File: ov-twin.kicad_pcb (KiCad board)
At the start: 4 copper layers, 64 x 64 mm, 101 parts, among them J1 USB_C_Receptacle_USB2.0, J2 Conn_01x02, J3 Conn_01x02, SW1 SW_SPST, SW2 SW_SPST, SW3 SW_SPST, SW4 SW_SPST, SW5 SW_SPST, SW6 SW_SPST, SW7 SW_SPST, SW8 SW_SPST, U1 NCP1117-3.3_SOT223, U2 RP2040, U3 RP2040, U4 W25Q128JVS, U5 W25Q128JVS, U7 LIS3DH, U8 SN74LVC1T45DBV, Y1 Crystal_GND24, Y2 Crystal_GND24, Y3 Crystal_GND24

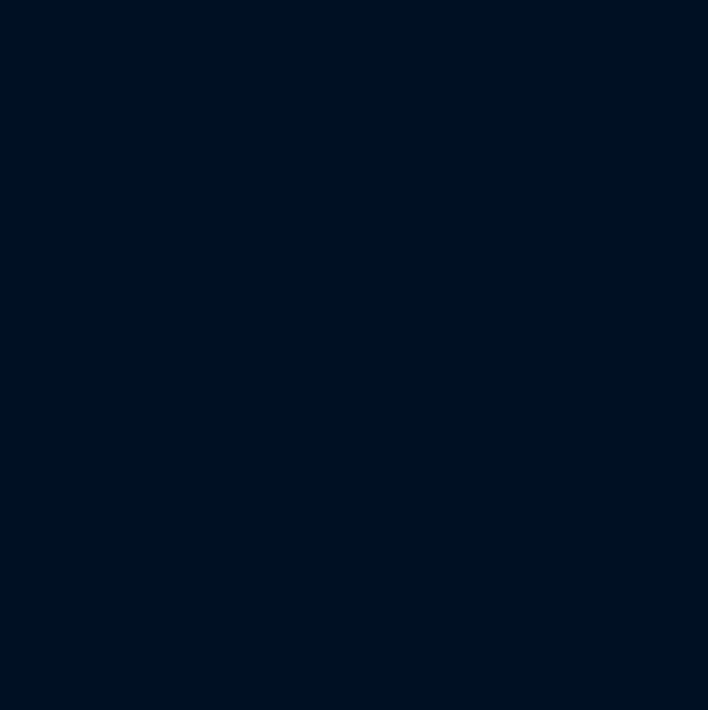
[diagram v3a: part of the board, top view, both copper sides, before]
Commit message: Add missing decoupling and such
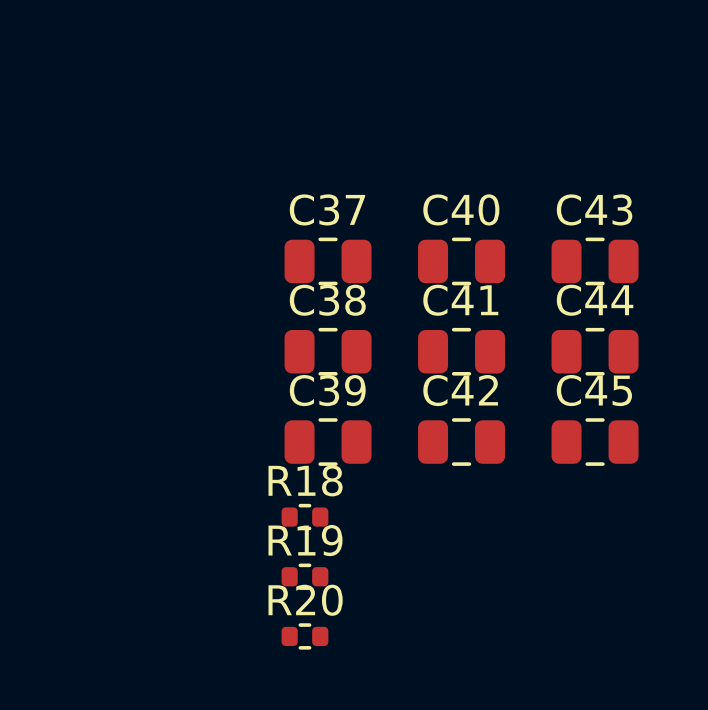
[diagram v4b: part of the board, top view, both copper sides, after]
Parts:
- added C37: 1u, Capacitor_SMD:C_0805_2012Metric, F.Cu at (233.9, 112.2)
- added C38: 1u, Capacitor_SMD:C_0805_2012Metric, F.Cu at (233.9, 115.2)
- added C39: 1u, Capacitor_SMD:C_0805_2012Metric, F.Cu at (233.9, 118.2)
- added C40: 10u, Capacitor_SMD:C_0805_2012Metric, F.Cu at (238.4, 112.2)
- added C41: 10u, Capacitor_SMD:C_0805_2012Metric, F.Cu at (238.4, 115.2)
- added C42: 10u, Capacitor_SMD:C_0805_2012Metric, F.Cu at (238.4, 118.2)
- added C43: 10u, Capacitor_SMD:C_0805_2012Metric, F.Cu at (242.8, 112.2)
- added C44: 10u, Capacitor_SMD:C_0805_2012Metric, F.Cu at (242.8, 115.2)
- added C45: 10u, Capacitor_SMD:C_0805_2012Metric, F.Cu at (242.8, 118.2)
- added R18: 10k, Resistor_SMD:R_0402_1005Metric, F.Cu at (233.2, 120.7)
- added R19: 10k, Resistor_SMD:R_0402_1005Metric, F.Cu at (233.2, 122.7)
- added R20: 10k, Resistor_SMD:R_0402_1005Metric, F.Cu at (233.2, 124.7)
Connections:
- U2 pad 12: unconnected-(U2-GPIO9-Pad12) -> /smartled-3v3
- U2 pad 13: unconnected-(U2-GPIO10-Pad13) -> /lis3dh-sdo-sa0
- U2 pad 14: unconnected-(U2-GPIO11-Pad14) -> /lis3dh-cs
- U2 pad 15: unconnected-(U2-GPIO12-Pad15) -> /lis3dh-scl-spc
- U2 pad 16: unconnected-(U2-GPIO13-Pad16) -> /lis3dh-sdi-sda
- U2 pad 17: unconnected-(U2-GPIO14-Pad17) -> /lis3dh-sdi-sda
- U2 pad 18: unconnected-(U2-GPIO15-Pad18) -> /lis3dh-scl-spc
- U2 pad 27: unconnected-(U2-GPIO16-Pad27) -> /lis3dh-int2
- U2 pad 28: unconnected-(U2-GPIO17-Pad28) -> /lis3dh-int1
- U2 pad 29: unconnected-(U2-GPIO18-Pad29) -> /pi-b-sw-1
- U2 pad 30: unconnected-(U2-GPIO19-Pad30) -> /pi-b-sw-2
- U2 pad 31: unconnected-(U2-GPIO20-Pad31) -> /pi-b-sw-3
- U2 pad 32: unconnected-(U2-GPIO21-Pad32) -> /pi-b-sw-4
- U2 pad 34: unconnected-(U2-GPIO22-Pad34) -> /pi-b-sw-5
- U2 pad 35: unconnected-(U2-GPIO23-Pad35) -> /pi-b-sw-6
- U2 pad 36: unconnected-(U2-GPIO24-Pad36) -> /pi-b-sw-7
- U2 pad 37: unconnected-(U2-GPIO25-Pad37) -> /pi-b-sw-8
- U2 pad 38: unconnected-(U2-GPIO26_ADC0-Pad38) -> /pi-b-pot

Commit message: That worked pretty well I thought!
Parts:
- C37, C38, C39: footprint Capacitor_SMD:C_0805_2012Metric -> Capacitor_SMD:C_0402_1005Metric
- moved C45 113.7 mm to (144.0, 62.0), turned to 180 degrees
- moved C44 102.0 mm to (144.0, 90.0), turned to 180 degrees
- moved C43 85.3 mm to (157.6, 110.0), turned to -90 degrees
- moved C37 65.9 mm to (172.0, 89.6), turned to 180 degrees
- moved R20 64.7 mm to (178.2, 90.6), turned to 90 degrees
- moved C40 63.1 mm to (200.0, 62.1)
- moved R19 62.8 mm to (179.2, 90.6), turned to 90 degrees
- moved C39 62.7 mm to (194.8, 69.2)
- moved R18 60.9 mm to (180.2, 90.6), turned to 90 degrees
- moved C38 56.5 mm to (194.8, 74.4)
- moved C42 53.4 mm to (185.6, 110.0), turned to 90 degrees
- moved C41 45.9 mm to (200.0, 90.0)
- moved C31 5.77 mm to (185.3, 72.5)
- moved R11 5.77 mm to (182.6, 73.0)
- moved R12 5.77 mm to (180.6, 73.0)
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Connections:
- C37 pad 1: +3V3 -> GND
- C37 pad 2: GND -> +3V3
- C38 pad 1: +3V3 -> GND
- C38 pad 2: GND -> +3V3
- C39 pad 1: +5V -> GND
- C39 pad 2: GND -> +5V
- U2 pad 11: unconnected-(U2-GPIO8-Pad11) -> /lis3dh-int1
- U2 pad 17: /lis3dh-sdi-sda -> unconnected-(U2-GPIO14-Pad17)
- U2 pad 18: /lis3dh-scl-spc -> unconnected-(U2-GPIO15-Pad18)
- U2 pad 27: /lis3dh-int2 -> unconnected-(U2-GPIO16-Pad27)
- U2 pad 28: /lis3dh-int1 -> unconnected-(U2-GPIO17-Pad28)
- U2 pad 29: /pi-b-sw-1 -> /pi-b-sw-4
- U2 pad 30: /pi-b-sw-2 -> /pi-b-sw-3
- U2 pad 31: /pi-b-sw-3 -> /pi-b-sw-2
- U2 pad 32: /pi-b-sw-4 -> /pi-b-sw-1
- U2 pad 9: unconnected-(U2-GPIO7-Pad9) -> /lis3dh-int2
- U8 pad 2: Net-(U8-DIR) -> GND
- U8 pad 3: /smartled-5v -> /smartled-5v0
- U8 pad 5: Net-(U8-DIR) -> GND
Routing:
- net +3V3: track 79.3 -> 375.6 mm, vias 33 -> 36
- net /smartled-3v3: track 8.34 -> 73.4 mm, vias 2 -> 5
- net /pi-b-sw-8: track 25.3 -> 71.0 mm, vias 2 -> 5
- net /pi-b-sw-6: track 19.2 -> 60.6 mm, vias 2 -> 6
- net /pi-b-sw-5: track 12.2 -> 53.0 mm, vias 2 -> 4
- net /pi-b-sw-4: track 43.8 -> 83.3 mm, vias 2 -> 5
- net /pi-b-sw-7: track 25.8 -> 64.0 mm, vias 2 -> 5
- net /pi-b-sw-2: track 46.3 -> 81.5 mm, vias 2 -> 5
- net /pi-b-sw-3: track 35.4 -> 65.4 mm, vias 2 -> 5
- net /lis3dh-cs: track 16.7 -> 46.0 mm, vias 2 -> 4
- net /lis3dh-sdo-sa0: track 16.6 -> 45.6 mm, vias 2 -> 4
- net /lis3dh-int2: track 13.0 -> 41.2 mm, vias 2 -> 4
- net /pi-b-pot: track 41.3 -> 69.4 mm, vias 1 -> 3
- net /lis3dh-int1: track 11.9 -> 38.7 mm, vias 2 -> 4
- net GND: track 49.3 -> 73.4 mm, vias 26 -> 30
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- removed copper zone on In2.Cu, net +3V3

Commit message: Updates
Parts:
- removed JP1: SolderJumper_2_Open, Jumper:SolderJumper-2_P1.3mm_Open_TrianglePad1.0x1.5mm
- removed R16, R17: 27, Resistor_SMD:R_0402_1005Metric
- added D25: LED3, LED_SMD:LED_0603_1608Metric, F.Cu at (141.5, 56.0)
- added D26: LED1, LED_SMD:LED_0603_1608Metric, F.Cu at (141.5, 57.5)
- added D27: LEDActive, LED_SMD:LED_0603_1608Metric, F.Cu at (139.5, 59.0)
- added G***: LOGO, LOGO, F.Cu at (141.0, 105.9)
- added J4: Conn_01x02, Connector_PinHeader_2.54mm:PinHeader_1x02_P2.54mm_Vertical, F.Cu at (160.4, 65.4)
- added R21: 220, Resistor_SMD:R_0402_1005Metric, F.Cu at (139.0, 56.0)
- added R22: 220, Resistor_SMD:R_0402_1005Metric, F.Cu at (139.0, 57.5)
- added R23: 470, Resistor_SMD:R_0402_1005Metric, F.Cu at (142.0, 59.0)
- added TP2: TestPoint, TestPoint:TestPoint_Pad_D1.5mm, B.Cu at (167.0, 65.0)
- added TP4: TestPoint, TestPoint:TestPoint_Pad_D1.5mm, B.Cu at (141.0, 58.0)
- C15, C16, C17, C19, C33, C34: value 27p -> 30pf; footprint Capacitor_SMD:C_0402_1005Metric -> Capacitor_SMD:C_0603_1608Metric
- D1, D10, D11, D12, D13, D14, D15, D16, D17, D18, D19, D2, D20, D21, D22, D23, D24, D3, D4, D5, D6, D7, D8, D9: value WS2812B -> ~
- moved J2 56.3 mm to (164.2, 65.4)
- moved J3 54.7 mm to (142.0, 65.1)
- moved C35 20.1 mm to (181.6, 54.6), turned to -90 degrees
- moved C34 14.8 mm to (144.2, 54.3)
- moved C15 14.4 mm to (147.4, 85.0), turned to 90 degrees
- moved C17 14.2 mm to (170.4, 85.2), turned to 90 degrees
- moved D14 14.2 mm to (153.5, 108.4), turned to 135 degrees
- moved D16 14.2 mm to (153.5, 91.6), turned to 45 degrees
- moved C14 14.1 mm to (173.8, 59.4)
- moved Y3 14.1 mm to (145.8, 57.4)
- moved C1 14.1 mm to (158.0, 72.2)
- moved C10 14.1 mm to (155.0, 70.7)
- moved C11 14.1 mm to (152.0, 70.7)
- moved C12 14.1 mm to (154.4, 83.1)
- moved C18 14.1 mm to (152.2, 62.5)
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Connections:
- C15 pad 1: /pi-a-xin -> GND
- C15 pad 2: GND -> /pi-a-xin
- C16 pad 1: Net-(C16-Pad1) -> GND
- C16 pad 2: GND -> Net-(C16-Pad2)
- C17 pad 1: /pi-b-xin -> GND
- C17 pad 2: GND -> /pi-b-xin
- C19 pad 1: Net-(C19-Pad1) -> GND
- C19 pad 2: GND -> Net-(C19-Pad2)
- C33 pad 1: /hub-xi -> GND
- C33 pad 2: GND -> /hub-xi
- C34 pad 1: Net-(JP1-A) -> GND
- C34 pad 2: GND -> Net-(C34-Pad2)
- D1 pad 1: +5V -> /smartled-5v0
- D1 pad 2: Net-(D1-DOUT) -> +5V
- D1 pad 3: GND -> Net-(D1-DOUT)
- D1 pad 4: /smartled-5v0 -> GND
- D10 pad 1: +5V -> Net-(D10-DIN)
- D10 pad 2: Net-(D10-DOUT) -> +5V
- D10 pad 3: GND -> Net-(D10-DOUT)
- D10 pad 4: Net-(D10-DIN) -> GND
- D11 pad 1: +5V -> Net-(D10-DOUT)
- D11 pad 2: Net-(D11-DOUT) -> +5V
- D11 pad 3: GND -> Net-(D11-DOUT)
- D11 pad 4: Net-(D10-DOUT) -> GND
- D12 pad 1: +5V -> Net-(D11-DOUT)
- D12 pad 2: Net-(D12-DOUT) -> +5V
- D12 pad 3: GND -> Net-(D12-DOUT)
- D12 pad 4: Net-(D11-DOUT) -> GND
- D13 pad 1: +5V -> Net-(D12-DOUT)
- D13 pad 2: Net-(D13-DOUT) -> +5V
- D13 pad 3: GND -> Net-(D13-DOUT)
- D13 pad 4: Net-(D12-DOUT) -> GND
- D14 pad 1: +5V -> Net-(D13-DOUT)
- D14 pad 2: Net-(D14-DOUT) -> +5V
- D14 pad 3: GND -> Net-(D14-DOUT)
- D14 pad 4: Net-(D13-DOUT) -> GND
- D15 pad 1: +5V -> Net-(D14-DOUT)
- D15 pad 2: Net-(D15-DOUT) -> +5V
- D15 pad 3: GND -> Net-(D15-DOUT)
- D15 pad 4: Net-(D14-DOUT) -> GND
- D16 pad 1: +5V -> Net-(D15-DOUT)
- D16 pad 2: Net-(D16-DOUT) -> +5V
- D16 pad 3: GND -> Net-(D16-DOUT)
- D16 pad 4: Net-(D15-DOUT) -> GND
- D17 pad 1: +5V -> Net-(D16-DOUT)
- D17 pad 2: Net-(D17-DOUT) -> +5V
- D17 pad 3: GND -> Net-(D17-DOUT)
- D17 pad 4: Net-(D16-DOUT) -> GND
- D18 pad 1: +5V -> Net-(D17-DOUT)
- D18 pad 2: Net-(D18-DOUT) -> +5V
- D18 pad 3: GND -> Net-(D18-DOUT)
- D18 pad 4: Net-(D17-DOUT) -> GND
- D19 pad 1: +5V -> Net-(D18-DOUT)
- D19 pad 2: Net-(D19-DOUT) -> +5V
- D19 pad 3: GND -> Net-(D19-DOUT)
- D19 pad 4: Net-(D18-DOUT) -> GND
- D2 pad 1: +5V -> Net-(D1-DOUT)
- D2 pad 2: Net-(D2-DOUT) -> +5V
- D2 pad 3: GND -> Net-(D2-DOUT)
- D2 pad 4: Net-(D1-DOUT) -> GND
- D20 pad 1: +5V -> Net-(D19-DOUT)
- D20 pad 2: Net-(D20-DOUT) -> +5V
- D20 pad 3: GND -> Net-(D20-DOUT)
- D20 pad 4: Net-(D19-DOUT) -> GND
- D21 pad 1: +5V -> Net-(D20-DOUT)
- D21 pad 2: Net-(D21-DOUT) -> +5V
- D21 pad 3: GND -> Net-(D21-DOUT)
- D21 pad 4: Net-(D20-DOUT) -> GND
- D22 pad 1: +5V -> Net-(D21-DOUT)
- D22 pad 2: Net-(D22-DOUT) -> +5V
- D22 pad 3: GND -> Net-(D22-DOUT)
- D22 pad 4: Net-(D21-DOUT) -> GND
- D23 pad 1: +5V -> Net-(D22-DOUT)
- D23 pad 2: Net-(D23-DOUT) -> +5V
- D23 pad 3: GND -> Net-(D23-DOUT)
- D23 pad 4: Net-(D22-DOUT) -> GND
- D24 pad 1: +5V -> Net-(D23-DOUT)
- D24 pad 2: unconnected-(D24-DOUT-Pad2) -> +5V
- D24 pad 3: GND -> unconnected-(D24-DOUT-Pad3)
- D24 pad 4: Net-(D23-DOUT) -> GND
- D3 pad 1: +5V -> Net-(D2-DOUT)
- D3 pad 2: Net-(D3-DOUT) -> +5V
- D3 pad 3: GND -> Net-(D3-DOUT)
- D3 pad 4: Net-(D2-DOUT) -> GND
- D4 pad 1: +5V -> Net-(D3-DOUT)
- D4 pad 2: Net-(D4-DOUT) -> +5V
- D4 pad 3: GND -> Net-(D4-DOUT)
- D4 pad 4: Net-(D3-DOUT) -> GND
- D5 pad 1: +5V -> Net-(D4-DOUT)
- D5 pad 2: Net-(D5-DOUT) -> +5V
- D5 pad 3: GND -> Net-(D5-DOUT)
- D5 pad 4: Net-(D4-DOUT) -> GND
- D6 pad 1: +5V -> Net-(D5-DOUT)
- D6 pad 2: Net-(D6-DOUT) -> +5V
- D6 pad 3: GND -> Net-(D6-DOUT)
- D6 pad 4: Net-(D5-DOUT) -> GND
- D7 pad 1: +5V -> Net-(D6-DOUT)
- D7 pad 2: Net-(D7-DOUT) -> +5V
- D7 pad 3: GND -> Net-(D7-DOUT)
- D7 pad 4: Net-(D6-DOUT) -> GND
- D8 pad 1: +5V -> Net-(D7-DOUT)
- D8 pad 2: Net-(D8-DOUT) -> +5V
- D8 pad 3: GND -> Net-(D8-DOUT)
- D8 pad 4: Net-(D7-DOUT) -> GND
- D9 pad 1: +5V -> Net-(D8-DOUT)
- D9 pad 2: Net-(D10-DIN) -> +5V
- D9 pad 3: GND -> Net-(D10-DIN)
- D9 pad 4: Net-(D8-DOUT) -> GND
- J2 pad 1: /~{USB_BOOT} -> +5V
- J3 pad 1: /~{USB_BOOT} -> /~{USB_BOOT_A}
- R11 pad 2: /~{USB_BOOT} -> /~{USB_BOOT_B}
- R13 pad 2: Net-(C19-Pad1) -> Net-(C19-Pad2)
- R15 pad 2: Net-(JP1-A) -> Net-(C34-Pad2)
- R5 pad 2: Net-(C16-Pad1) -> Net-(C16-Pad2)
- R9 pad 2: /~{USB_BOOT} -> /~{USB_BOOT_A}
- U6 pad 13: unconnected-(U6-LED3/SCL-Pad13) -> /usb-led3
- U6 pad 14: Net-(U6-DMU) -> /USB_D-
- U6 pad 15: Net-(U6-DPU) -> /USB_D+
- U6 pad 18: unconnected-(U6-PSELF-Pad18) -> Net-(U6-PSELF)
- U6 pad 19: +5V -> +3V3
- U6 pad 21: unconnected-(U6-LED4/SDA-Pad21) -> /usb-led4
- U6 pad 22: unconnected-(U6-LED1-Pad22) -> /usb-led1
- U6 pad 23: unconnected-(U6-LED2-Pad23) -> /usb-led2
- Y1 pad 3: Net-(C16-Pad1) -> Net-(C16-Pad2)
- Y2 pad 3: Net-(C19-Pad1) -> Net-(C19-Pad2)
- Y3 pad 3: Net-(JP1-A) -> Net-(C34-Pad2)
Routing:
- net +5V: track 325.4 -> 376.2 mm, vias 9 -> 11
- net /usb-led2: track 0.00 -> 23.3 mm, vias 0 -> 2
- net +3V3: track 375.6 -> 394.1 mm, vias 36 -> 37
- net Net-(U6-PSELF): track 0.00 -> 17.8 mm, vias 0 -> 2
- net /usb-led4: track 0.00 -> 15.1 mm, vias 0 -> 2
- net /usb-led1: track 0.00 -> 14.9 mm, vias 0 -> 2
- net GND: track 73.4 -> 61.5 mm, vias 30 -> 125
- net /~{USB_BOOT_A}: track 0.00 -> 9.58 mm, vias 0 -> 1
- net /~{USB_BOOT_B}: track 0.00 -> 7.80 mm, vias 0 -> 2
- net Net-(JP1-A): track 6.00 -> 0.00 mm
- net Net-(C19-Pad2): track 0.00 -> 3.81 mm
- net Net-(C16-Pad2): track 0.00 -> 3.81 mm
- net Net-(C34-Pad2): track 0.00 -> 3.45 mm
- net /smartled-5v0: track 14.6 -> 17.5 mm
- net Net-(D8-DOUT): track 44.2 -> 47.1 mm
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- added copper zone on In1.Cu, net GND
- added copper zone on In2.Cu, net GND
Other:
- board text added: "1"
- board text added: "2"
- board text added: "3"
- board text added: "3v3"
- board text added: "4"
- board text added: "5"
- board text added: "5v0"
- board text added: "6"
- board text added: "7"
- board text added: "8"
- board text added: "act"
- board text added: "ams1117"
- board text added: "boot"
- board text added: "ch334"
- board text added: "dbg"
- board text added: "debug probe"
- board text added: "lis3dh"
- board text added: "pself"
- board text added: "sn74lvc1"
- board text added: "target"
- board text added: "tgt"
- board text added: "twin trainer prototype - rev 01 march 2024"
- board text added: "usb-boot"

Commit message: Second order
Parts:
- removed C33, C34: 30pf, Capacitor_SMD:C_0603_1608Metric
- removed R15: 1k, Resistor_SMD:R_0402_1005Metric
- added T1: ~, ov-twin:tooling-hole, F.Cu at (132.0, 52.0)
- added T2: ~, ov-twin:tooling-hole, F.Cu at (192.0, 112.0)
- added TP1: TestPoint, TestPoint:TestPoint_Pad_D1.5mm, B.Cu at (174.0, 86.0)
- added TP3: TestPoint, TestPoint:TestPoint_Pad_D1.5mm, B.Cu at (171.0, 86.0)
- moved C45 3.94 mm to (137.2, 54.3), turned to 0 degrees
- moved C40 3.88 mm to (186.8, 54.3), turned to 180 degrees
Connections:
- Y3 pad 3: Net-(C34-Pad2) -> /hub-xo
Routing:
- net Net-(U3-RUN): track 2.65 -> 17.6 mm, vias 0 -> 2
- net +5V: track 376.2 -> 371.5 mm
- net Net-(C34-Pad2): track 3.45 -> 0.00 mm
- net /hub-xo: track 2.73 -> 5.13 mm
- net GND: track 61.5 -> 59.2 mm, vias 125 -> 127
- net /hub-xi: track 4.50 -> 2.56 mm
- net +3V3: track 394.1 -> 393.4 mm
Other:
- outline, holes or cut-outs redrawn
- board text added: "board #"
- board text added: "onevariable.com"
- board text added: "tgt run"
- board text added: "this side down"
- board text added: "twin trainer prototype - rev 02 april 2024"
- board text removed: "twin trainer prototype - rev 01 march 2024"
